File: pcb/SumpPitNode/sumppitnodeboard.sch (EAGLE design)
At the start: 35 parts, among them IC1 7805T

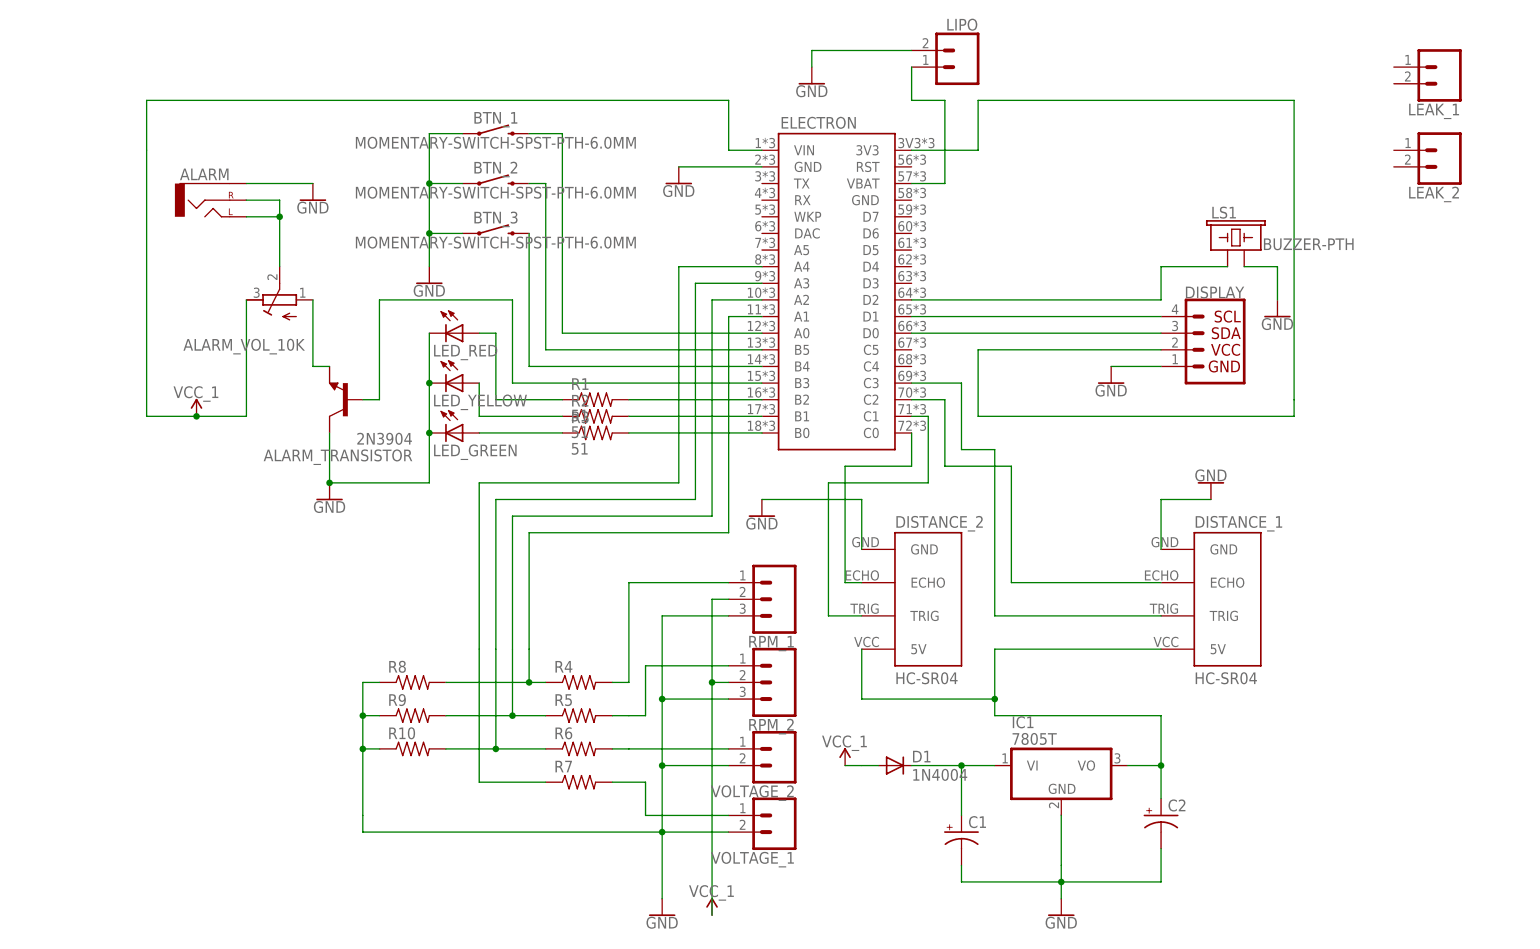
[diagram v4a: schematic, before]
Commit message: Fix, add multiple vcc, create base sch.
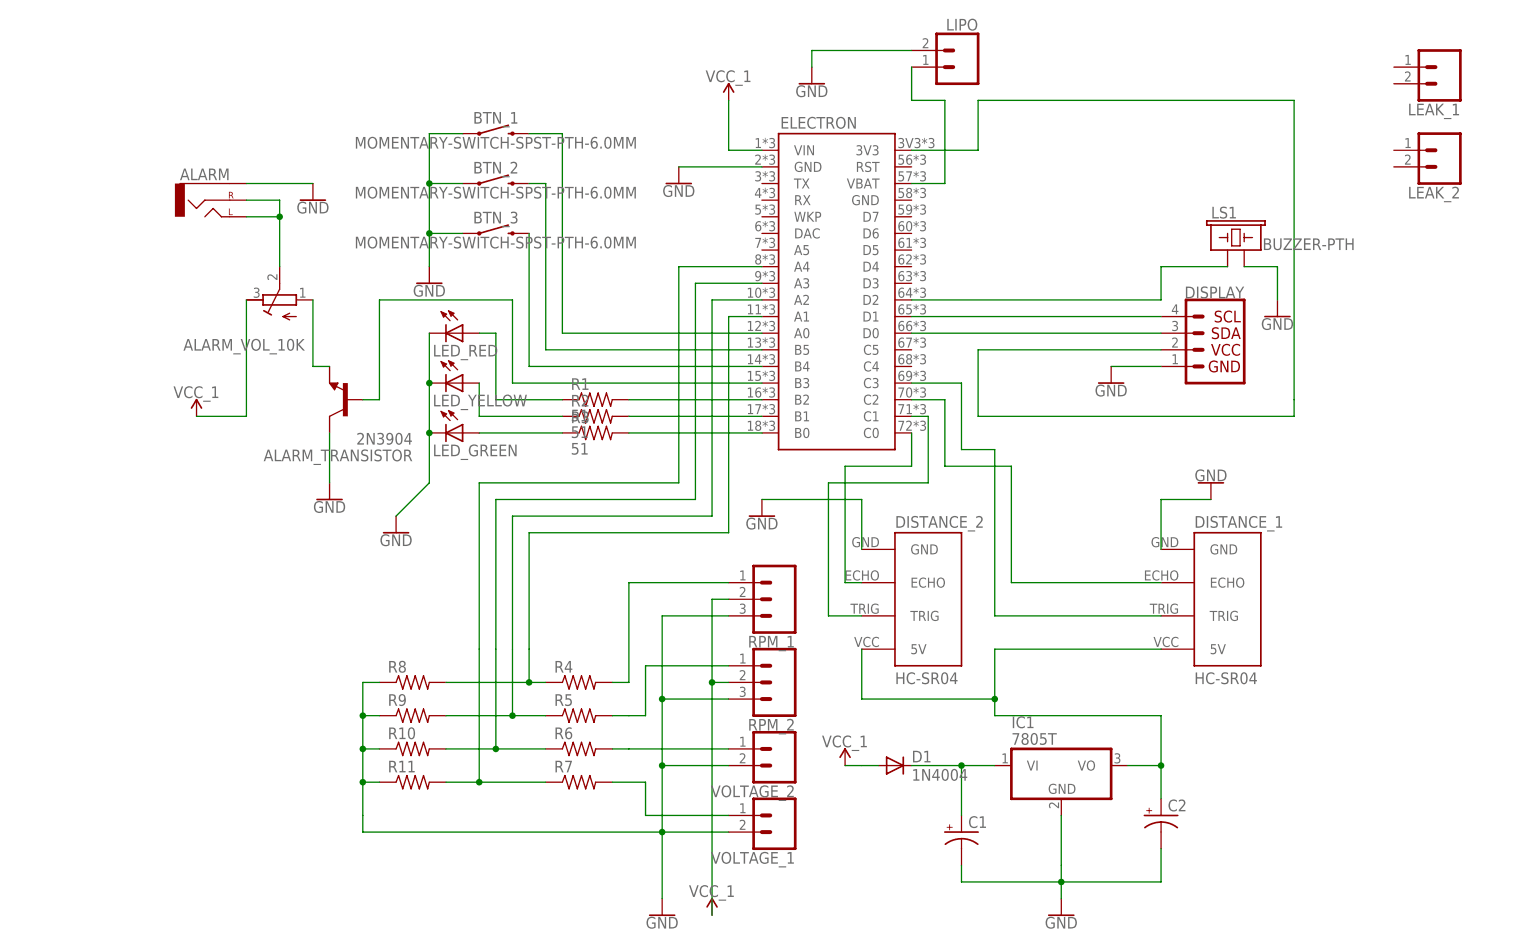
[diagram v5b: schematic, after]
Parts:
- added R11: (no value), resistor:R-US_0204/5
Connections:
- removed net B$11: ALARM_VOL_10K.E, ELECTRON.VIN
- net GND: now also R11.1
- net N$31: now also R11.2
- net VCC_1: now also ALARM_VOL_10K.E, ELECTRON.VIN
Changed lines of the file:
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@@
 <part name="R10" library="resistor" library_urn="urn:adsk.eagle:library:348" deviceset="R-US_" device="0204/5" package3d_urn="urn:adsk.eagle:package:25955/1"/>
 <part name="VCC_12V2" library="SparkFun-PowerSymbols" library_urn="urn:adsk.eagle:library:530" deviceset="VCC_1" device=""/>
+<part name="GND12" library="SparkFun-PowerSymbols" library_urn="urn:adsk.eagle:library:530" deviceset="GND" device=""/>
+<part name="VCC_12V3" library="SparkFun-PowerSymbols" library_urn="urn:adsk.eagle:library:530" deviceset="VCC_1" device=""/>
+<part name="R11" library="resistor" library_urn="urn:adsk.eagle:library:348" deviceset="R-US_" device="0204/5" package3d_urn="urn:adsk.eagle:package:25955/1"/>
 </parts>
 <sheets>
@@
 <instance part="R10" gate="G$1" x="-99.06" y="-10.16"/>
 <instance part="VCC_12V2" gate="G$2" x="-33.02" y="-12.7"/>
+<instance part="GND12" gate="1" x="-101.6" y="22.86"/>
+<instance part="VCC_12V3" gate="G$2" x="-50.8" y="88.9"/>
+<instance part="R11" gate="G$1" x="-99.06" y="-15.24"/>
 </instances>
 <busses>
 </busses>
 <nets>
-<net name="B$11" class="0">
-<segment>
-<pinref part="VCC_12V" gate="G$2" pin="VCC_1"/>
-<wire x1="-124.46" y1="58.42" x2="-124.46" y2="40.64" width="0.1524" layer="91"/>
-<wire x1="-124.46" y1="40.64" x2="-132.08" y2="40.64" width="0.1524" layer="91"/>
-<pinref part="ALARM_VOL_10K" gate="G$1" pin="E"/>
-<wire x1="-132.08" y1="40.64" x2="-139.7" y2="40.64" width="0.1524" layer="91"/>
-<junction x="-132.08" y="40.64"/>
-<wire x1="-139.7" y1="40.64" x2="-139.7" y2="81.28" width="0.1524" layer="91"/>
-<wire x1="-139.7" y1="81.28" x2="-139.7" y2="88.9" width="0.1524" layer="91"/>
-<wire x1="-139.7" y1="88.9" x2="-50.8" y2="88.9" width="0.1524" layer="91"/>
-<wire x1="-50.8" y1="88.9" x2="-50.8" y2="81.28" width="0.1524" layer="91"/>
-<pinref part="ELECTRON" gate="G$1" pin="VIN"/>
-<wire x1="-50.8" y1="81.28" x2="-45.72" y2="81.28" width="0.1524" layer="91"/>
-</segment>
-</net>
 <net name="N$1" class="0">
 <segment>
@@
 </segment>
 <segment>
+<pinref part="ALARM_TRANSISTOR" gate="G1" pin="C"/>
 <pinref part="GND2" gate="1" pin="GND"/>
-<pinref part="ALARM_TRANSISTOR" gate="G1" pin="C"/>
 <wire x1="-111.76" y1="30.48" x2="-111.76" y2="38.1" width="0.1524" layer="91"/>
-<pinref part="LED_RED" gate="G$1" pin="C"/>
-<pinref part="LED_YELLOW" gate="G$1" pin="C"/>
-<wire x1="-96.52" y1="53.34" x2="-96.52" y2="45.72" width="0.1524" layer="91"/>
-<pinref part="LED_GREEN" gate="G$1" pin="C"/>
-<wire x1="-96.52" y1="45.72" x2="-96.52" y2="38.1" width="0.1524" layer="91"/>
-<junction x="-96.52" y="45.72"/>
-<wire x1="-96.52" y1="38.1" x2="-96.52" y2="30.48" width="0.1524" layer="91"/>
-<wire x1="-96.52" y1="30.48" x2="-111.76" y2="30.48" width="0.1524" layer="91"/>
-<junction x="-96.52" y="38.1"/>
-<junction x="-111.76" y="30.48"/>
 </segment>
 <segment>
@@
 <wire x1="-104.14" y1="-5.08" x2="-106.68" y2="-5.08" width="0.1524" layer="91"/>
 <junction x="-106.68" y="-5.08"/>
-<wire x1="-106.68" y1="-10.16" x2="-106.68" y2="-20.32" width="0.1524" layer="91"/>
+<wire x1="-106.68" y1="-10.16" x2="-106.68" y2="-15.24" width="0.1524" layer="91"/>
 <junction x="-106.68" y="-10.16"/>
+<wire x1="-106.68" y1="-15.24" x2="-106.68" y2="-20.32" width="0.1524" layer="91"/>
 <wire x1="-106.68" y1="-20.32" x2="-106.68" y2="-22.86" width="0.1524" layer="91"/>
 <pinref part="VOLTAGE_1" gate="G$1" pin="2"/>
@@
 <wire x1="-50.8" y1="-12.7" x2="-60.96" y2="-12.7" width="0.1524" layer="91"/>
 <junction x="-60.96" y="-12.7"/>
+<pinref part="R11" gate="G$1" pin="1"/>
+<wire x1="-104.14" y1="-15.24" x2="-106.68" y2="-15.24" width="0.1524" layer="91"/>
+<junction x="-106.68" y="-15.24"/>
+</segment>
+<segment>
+<pinref part="LED_RED" gate="G$1" pin="C"/>
+<pinref part="LED_YELLOW" gate="G$1" pin="C"/>
+<wire x1="-96.52" y1="53.34" x2="-96.52" y2="45.72" width="0.1524" layer="91"/>
+<pinref part="LED_GREEN" gate="G$1" pin="C"/>
+<wire x1="-96.52" y1="45.72" x2="-96.52" y2="38.1" width="0.1524" layer="91"/>
+<junction x="-96.52" y="45.72"/>
+<wire x1="-96.52" y1="38.1" x2="-96.52" y2="30.48" width="0.1524" layer="91"/>
+<junction x="-96.52" y="38.1"/>
+<pinref part="GND12" gate="1" pin="GND"/>
+<wire x1="-96.52" y1="30.48" x2="-101.6" y2="25.4" width="0.1524" layer="91"/>
 </segment>
 </net>
@@
 <pinref part="VCC_12V2" gate="G$2" pin="VCC_1"/>
 <wire x1="-30.48" y1="-12.7" x2="-33.02" y2="-12.7" width="0.1524" layer="91"/>
+</segment>
+<segment>
+<pinref part="ELECTRON" gate="G$1" pin="VIN"/>
+<pinref part="VCC_12V3" gate="G$2" pin="VCC_1"/>
+<wire x1="-50.8" y1="88.9" x2="-50.8" y2="81.28" width="0.1524" layer="91"/>
+<wire x1="-50.8" y1="81.28" x2="-45.72" y2="81.28" width="0.1524" layer="91"/>
+</segment>
+<segment>
+<pinref part="VCC_12V" gate="G$2" pin="VCC_1"/>
+<wire x1="-124.46" y1="58.42" x2="-124.46" y2="40.64" width="0.1524" layer="91"/>
+<wire x1="-124.46" y1="40.64" x2="-132.08" y2="40.64" width="0.1524" layer="91"/>
+<pinref part="ALARM_VOL_10K" gate="G$1" pin="E"/>
 </segment>
 </net>
@@
 <pinref part="ELECTRON" gate="G$1" pin="A4"/>
 <wire x1="-58.42" y1="63.5" x2="-45.72" y2="63.5" width="0.1524" layer="91"/>
-</segment>
-</net>
+<wire x1="-88.9" y1="-15.24" x2="-93.98" y2="-15.24" width="0.1524" layer="91"/>
+<junction x="-88.9" y="-15.24"/>
+<pinref part="R11" gate="G$1" pin="2"/>
+</segment>
+</net>

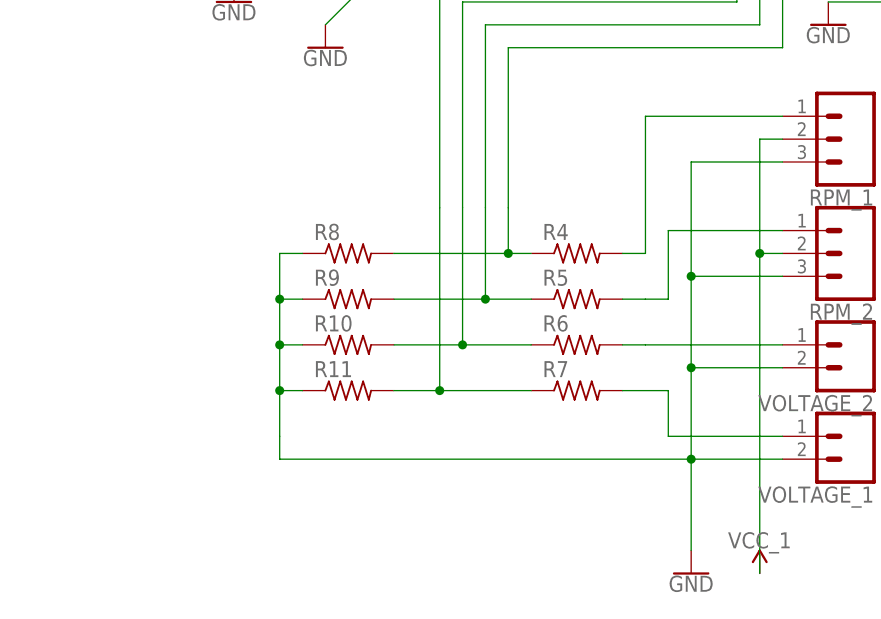
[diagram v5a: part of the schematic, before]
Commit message: Generate board, connect more sensors.
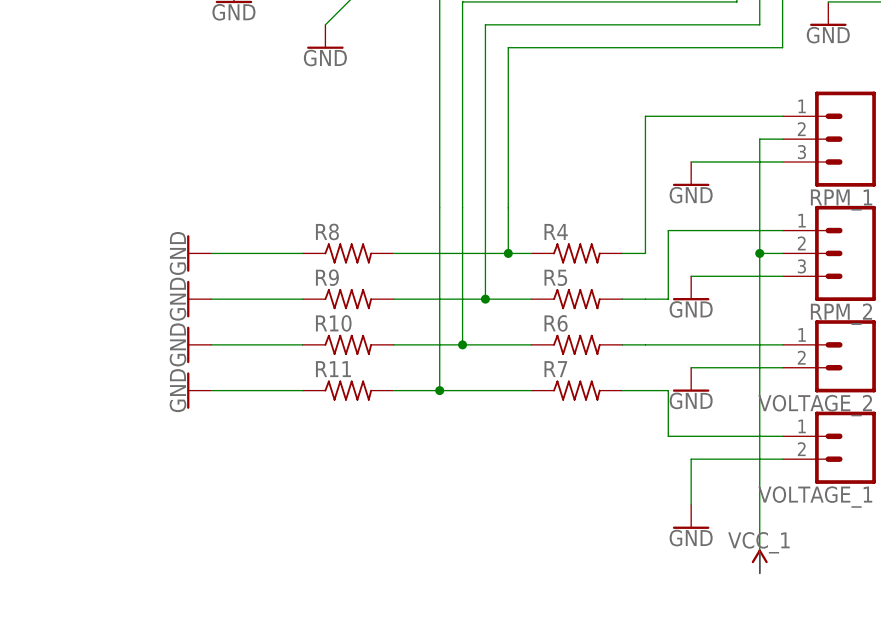
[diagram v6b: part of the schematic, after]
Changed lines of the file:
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@@
 <part name="VCC_12V3" library="SparkFun-PowerSymbols" library_urn="urn:adsk.eagle:library:530" deviceset="VCC_1" device=""/>
 <part name="R11" library="resistor" library_urn="urn:adsk.eagle:library:348" deviceset="R-US_" device="0204/5" package3d_urn="urn:adsk.eagle:package:25955/1"/>
+<part name="GND13" library="SparkFun-PowerSymbols" library_urn="urn:adsk.eagle:library:530" deviceset="GND" device=""/>
+<part name="GND14" library="SparkFun-PowerSymbols" library_urn="urn:adsk.eagle:library:530" deviceset="GND" device=""/>
+<part name="GND15" library="SparkFun-PowerSymbols" library_urn="urn:adsk.eagle:library:530" deviceset="GND" device=""/>
+<part name="GND16" library="SparkFun-PowerSymbols" library_urn="urn:adsk.eagle:library:530" deviceset="GND" device=""/>
+<part name="GND17" library="SparkFun-PowerSymbols" library_urn="urn:adsk.eagle:library:530" deviceset="GND" device=""/>
+<part name="GND18" library="SparkFun-PowerSymbols" library_urn="urn:adsk.eagle:library:530" deviceset="GND" device=""/>
+<part name="GND19" library="SparkFun-PowerSymbols" library_urn="urn:adsk.eagle:library:530" deviceset="GND" device=""/>
 </parts>
 <sheets>
@@
 <instance part="GND10" gate="1" x="33.02" y="55.88"/>
 <instance part="VCC_12V1" gate="G$2" x="-53.34" y="-35.56"/>
-<instance part="GND11" gate="1" x="-60.96" y="-35.56"/>
+<instance part="GND11" gate="1" x="-60.96" y="-30.48"/>
 <instance part="R4" gate="G$1" x="-73.66" y="0"/>
 <instance part="R5" gate="G$1" x="-73.66" y="-5.08"/>
@@
 <instance part="VCC_12V3" gate="G$2" x="-50.8" y="88.9"/>
 <instance part="R11" gate="G$1" x="-99.06" y="-15.24"/>
+<instance part="GND13" gate="1" x="-116.84" y="0" rot="R270"/>
+<instance part="GND14" gate="1" x="-116.84" y="-5.08" rot="R270"/>
+<instance part="GND15" gate="1" x="-116.84" y="-10.16" rot="R270"/>
+<instance part="GND16" gate="1" x="-116.84" y="-15.24" rot="R270"/>
+<instance part="GND17" gate="1" x="-60.96" y="-15.24"/>
+<instance part="GND18" gate="1" x="-60.96" y="-5.08"/>
+<instance part="GND19" gate="1" x="-60.96" y="7.62"/>
 </instances>
 <busses>
@@
 <segment>
 <pinref part="GND11" gate="1" pin="GND"/>
-<wire x1="-60.96" y1="-33.02" x2="-60.96" y2="-22.86" width="0.1524" layer="91"/>
-<pinref part="RPM_2" gate="J$1" pin="3"/>
-<wire x1="-60.96" y1="-22.86" x2="-60.96" y2="-12.7" width="0.1524" layer="91"/>
-<wire x1="-60.96" y1="-12.7" x2="-60.96" y2="-2.54" width="0.1524" layer="91"/>
-<wire x1="-60.96" y1="-2.54" x2="-50.8" y2="-2.54" width="0.1524" layer="91"/>
-<pinref part="RPM_1" gate="J$1" pin="3"/>
-<wire x1="-50.8" y1="10.16" x2="-60.96" y2="10.16" width="0.1524" layer="91"/>
-<wire x1="-60.96" y1="10.16" x2="-60.96" y2="-2.54" width="0.1524" layer="91"/>
-<junction x="-60.96" y="-2.54"/>
-<pinref part="R10" gate="G$1" pin="1"/>
-<wire x1="-104.14" y1="-10.16" x2="-106.68" y2="-10.16" width="0.1524" layer="91"/>
-<wire x1="-106.68" y1="-10.16" x2="-106.68" y2="-5.08" width="0.1524" layer="91"/>
-<wire x1="-106.68" y1="-5.08" x2="-106.68" y2="0" width="0.1524" layer="91"/>
-<pinref part="R8" gate="G$1" pin="1"/>
-<wire x1="-106.68" y1="0" x2="-104.14" y2="0" width="0.1524" layer="91"/>
-<pinref part="R9" gate="G$1" pin="1"/>
-<wire x1="-104.14" y1="-5.08" x2="-106.68" y2="-5.08" width="0.1524" layer="91"/>
-<junction x="-106.68" y="-5.08"/>
-<wire x1="-106.68" y1="-10.16" x2="-106.68" y2="-15.24" width="0.1524" layer="91"/>
-<junction x="-106.68" y="-10.16"/>
-<wire x1="-106.68" y1="-15.24" x2="-106.68" y2="-20.32" width="0.1524" layer="91"/>
-<wire x1="-106.68" y1="-20.32" x2="-106.68" y2="-22.86" width="0.1524" layer="91"/>
+<wire x1="-60.96" y1="-27.94" x2="-60.96" y2="-22.86" width="0.1524" layer="91"/>
 <pinref part="VOLTAGE_1" gate="G$1" pin="2"/>
-<wire x1="-106.68" y1="-22.86" x2="-60.96" y2="-22.86" width="0.1524" layer="91"/>
-<junction x="-60.96" y="-22.86"/>
 <wire x1="-60.96" y1="-22.86" x2="-50.8" y2="-22.86" width="0.1524" layer="91"/>
-<pinref part="VOLTAGE_2" gate="G$1" pin="2"/>
-<wire x1="-50.8" y1="-12.7" x2="-60.96" y2="-12.7" width="0.1524" layer="91"/>
-<junction x="-60.96" y="-12.7"/>
-<pinref part="R11" gate="G$1" pin="1"/>
-<wire x1="-104.14" y1="-15.24" x2="-106.68" y2="-15.24" width="0.1524" layer="91"/>
-<junction x="-106.68" y="-15.24"/>
 </segment>
 <segment>
@@
 <wire x1="-96.52" y1="30.48" x2="-101.6" y2="25.4" width="0.1524" layer="91"/>
 </segment>
+<segment>
+<pinref part="GND13" gate="1" pin="GND"/>
+<pinref part="R8" gate="G$1" pin="1"/>
+<wire x1="-114.3" y1="0" x2="-104.14" y2="0" width="0.1524" layer="91"/>
+</segment>
+<segment>
+<pinref part="R9" gate="G$1" pin="1"/>
+<pinref part="GND14" gate="1" pin="GND"/>
+<wire x1="-104.14" y1="-5.08" x2="-114.3" y2="-5.08" width="0.1524" layer="91"/>
+</segment>
+<segment>
+<pinref part="GND15" gate="1" pin="GND"/>
+<pinref part="R10" gate="G$1" pin="1"/>
+<wire x1="-114.3" y1="-10.16" x2="-104.14" y2="-10.16" width="0.1524" layer="91"/>
+</segment>
+<segment>
+<pinref part="R11" gate="G$1" pin="1"/>
+<pinref part="GND16" gate="1" pin="GND"/>
+<wire x1="-104.14" y1="-15.24" x2="-114.3" y2="-15.24" width="0.1524" layer="91"/>
+</segment>
+<segment>
+<pinref part="RPM_1" gate="J$1" pin="3"/>
+<wire x1="-50.8" y1="10.16" x2="-60.96" y2="10.16" width="0.1524" layer="91"/>
+<pinref part="GND19" gate="1" pin="GND"/>
+</segment>
+<segment>
+<pinref part="RPM_2" gate="J$1" pin="3"/>
+<wire x1="-60.96" y1="-2.54" x2="-50.8" y2="-2.54" width="0.1524" layer="91"/>
+<pinref part="GND18" gate="1" pin="GND"/>
+</segment>
+<segment>
+<pinref part="VOLTAGE_2" gate="G$1" pin="2"/>
+<wire x1="-50.8" y1="-12.7" x2="-60.96" y2="-12.7" width="0.1524" layer="91"/>
+<pinref part="GND17" gate="1" pin="GND"/>
+</segment>
 </net>
 <net name="N$2" class="0">
@@
 <wire x1="-78.74" y1="0" x2="-81.28" y2="0" width="0.1524" layer="91"/>
 <wire x1="-81.28" y1="0" x2="-81.28" y2="5.08" width="0.1524" layer="91"/>
-<wire x1="-81.28" y1="0" x2="-93.98" y2="0" width="0.1524" layer="91"/>
-<junction x="-81.28" y="0"/>
-<pinref part="R8" gate="G$1" pin="2"/>
 <wire x1="-81.28" y1="5.08" x2="-81.28" y2="22.86" width="0.1524" layer="91"/>
 <wire x1="-81.28" y1="22.86" x2="-50.8" y2="22.86" width="0.1524" layer="91"/>
@@
 <pinref part="ELECTRON" gate="G$1" pin="A1"/>
 <wire x1="-50.8" y1="55.88" x2="-45.72" y2="55.88" width="0.1524" layer="91"/>
+<pinref part="R8" gate="G$1" pin="2"/>
+<wire x1="-81.28" y1="0" x2="-93.98" y2="0" width="0.1524" layer="91"/>
+<junction x="-81.28" y="0"/>
 </segment>
 </net>
@@
 </sheet>
 </sheets>
+<errors>
+</errors>
 </schematic>
 </drawing>
